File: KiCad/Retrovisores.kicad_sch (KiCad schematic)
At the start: 50 parts, among them J1 Conn_01x02_Pin, J2 Conn_PIC_ICSP_ICD, M1 Motor_DC, M2 Motor_DC, M3 Motor_DC, Q1 AO3400A, Q10 AO3401A, Q11 AO3400A, Q12 AO3401A, Q2 AO3400A, Q3 AO3401A, Q4 AO3401A, Q5 AO3400A, Q6 AO3401A, Q7 AO3400A, Q8 AO3401A, Q9 AO3400A, SW1 SW_SPST, SW10 SW_Push, SW2 SW_SPST, SW3 SW_SPST, SW4 SW_SPST, SW5 SW_SPST, SW6 SW_SPST, SW7 SW_Push, SW8 SW_Push, SW9 SW_Push, U1 PIC32MX250F128D-IPT, U2 SN65HVD232, U3 FT232RL, U4 LT1117-3.3, U5 TSR3-2450N, U6 VL53L1CXV0FY1

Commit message: he ordenat tot
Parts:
- removed C1, C2: C, symbol Device:C
- removed C3: 100 nF, symbol Device:C
- removed D1: LED, symbol Device:LED
- removed J1: Conn_01x02_Pin, symbol Connector:Conn_01x02_Pin
- removed J2: Conn_PIC_ICSP_ICD, symbol Connector:Conn_PIC_ICSP_ICD
- removed M1, M2, M3: Motor_DC, symbol Motor:Motor_DC
- removed Q1, Q11, Q2, Q5, Q7, Q9: AO3400A, Package_TO_SOT_SMD:SOT-23, symbol Transistor_FET:AO3400A
- removed Q10, Q12, Q3, Q4, Q6, Q8: AO3401A, Package_TO_SOT_SMD:SOT-23, symbol Transistor_FET:AO3401A
- removed R1, R10, R11, R12, R2, R3, R4, R5, R6, R7, R8, R9: R, symbol Device:R
- removed R13: 1k, symbol Device:R
- removed SW1, SW2, SW3, SW4, SW5, SW6: SW_SPST, symbol Switch:SW_SPST
- removed SW10, SW7, SW8, SW9: SW_Push, symbol Switch:SW_Push
- removed U1: PIC32MX250F128D-IPT, Package_QFP:TQFP-44_10x10mm_P0.8mm, symbol MCU_Microchip_PIC32:PIC32MX250F128D-IPT
- removed U2: SN65HVD232, Package_SO:SOIC-8_3.9x4.9mm_P1.27mm, symbol Interface_CAN_LIN:SN65HVD232
- removed U3: FT232RL, Package_SO:SSOP-28_5.3x10.2mm_P0.65mm, symbol Interface_USB:FT232RL
- removed U4: LT1117-3.3, symbol Regulator_Linear:LT1117-3.3
- removed U5: TSR3-2450N, Converter_DCDC:Converter_DCDC_TRACO_TSR2-24xxN_TSR2-24xxxN_THT, symbol Converter_DCDC:TSR3-2450N
- removed U6: VL53L1CXV0FY1, Sensor_Distance:ST_VL53L1x, symbol Sensor_Distance:VL53L1CXV0FY1
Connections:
- no-connect marks 2 -> 0
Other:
- added sheet Alimentacion (alimentacion.kicad_sch)
- added sheet BOTONERA (BOTONERA.kicad_sch)
- added sheet CAN (BUS CAN.kicad_sch)
- added sheet FINALCARRERA (FC.kicad_sch)
- added sheet MICRO (MICRO.kicad_sch)
- added sheet PROGRAMADOR (PROGRAMADOR.kicad_sch)
- added sheet SENSOR (SENSOR_PROX_sch.kicad_sch)
- added sheet USART (USART.kicad_sch)
- added sheet drivers motor (driver_sch.kicad_sch)

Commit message: calefactor
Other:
- added sheet Calefactor (Calefactor_sch.kicad_sch)
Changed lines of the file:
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@@
 	(paper "A4")
+	(sheet
+		(at 153.67 58.42)
+		(size 35.56 20.32)
+		(exclude_from_sim no)
+		(in_bom yes)
+		(on_board yes)
+		(dnp no)
+		(fields_autoplaced yes)
+		(stroke
+			(width 0.1524)
+			(type solid)
+		)
+		(fill
+			(color 0 0 0 0.0000)
+		)
+		(property "Sheetname" "Calefactor"
+			(at 153.67 57.7084 0)
+			(effects
+				(font
+					(size 1.27 1.27)
+				)
+				(justify left bottom)
+			)
+		)
+		(property "Sheetfile" "Calefactor_sch.kicad_sch"
+			(at 153.67 79.3246 0)
+			(effects
+				(font
+					(size 1.27 1.27)
+				)
+				(justify left top)
+			)
+		)
+		(instances
+			(project "Retrovisores"
+				(path "/9b9f005f-0621-4675-bd4e-683e7082b120"
+					(page "11")
+				)
+			)
+		)
+	)
 	(sheet
 		(at 67.31 24.13)

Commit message: calefactor-Usart
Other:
- removed sheet USART
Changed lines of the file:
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@@
-		)
-	)
-	(sheet
-		(at 237.49 24.13)
-		(size 34.29 22.86)
-		(exclude_from_sim no)
-		(in_bom yes)
-		(on_board yes)
-		(dnp no)
-		(fields_autoplaced yes)
-		(stroke
-			(width 0.1524)
-			(type solid)
-		)
-		(fill
-			(color 0 0 0 0.0000)
-		)
-		(property "Sheetname" "USART"
-			(at 237.49 23.4184 0)
-			(effects
-				(font
-					(size 1.27 1.27)
-				)
-				(justify left bottom)
-			)
-		)
-		(property "Sheetfile" "USART.kicad_sch"
-			(at 237.49 47.5746 0)
-			(effects
-				(font
-					(size 1.27 1.27)
-				)
-				(justify left top)
-			)
-		)
-		(instances
-			(project "Retrovisores"
-				(path "/9b9f005f-0621-4675-bd4e-683e7082b120"
-					(page "7")
-				)
-			)
 		)
 	)

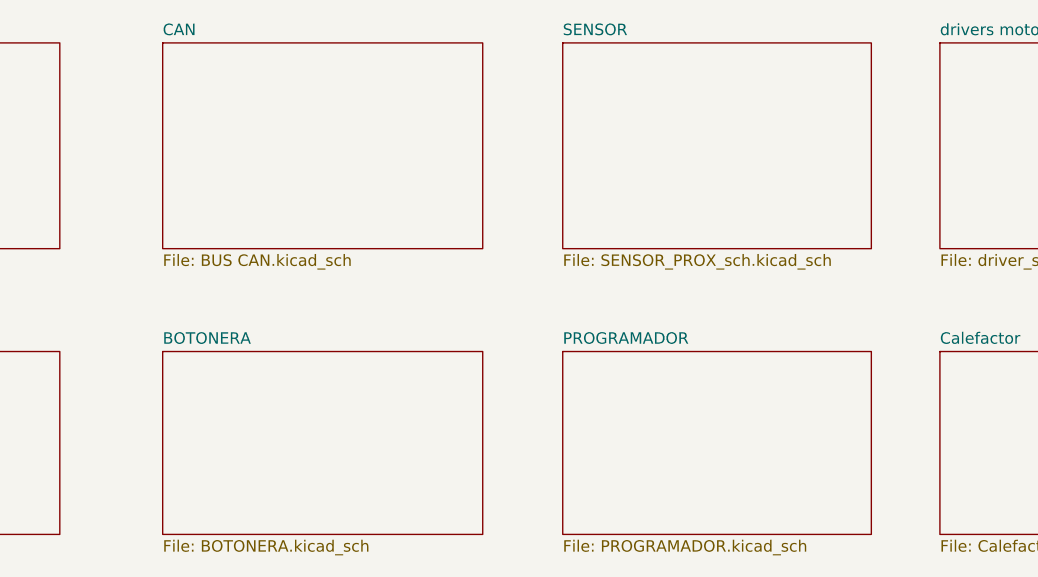
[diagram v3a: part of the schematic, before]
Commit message: canvis organització y reles calefactor
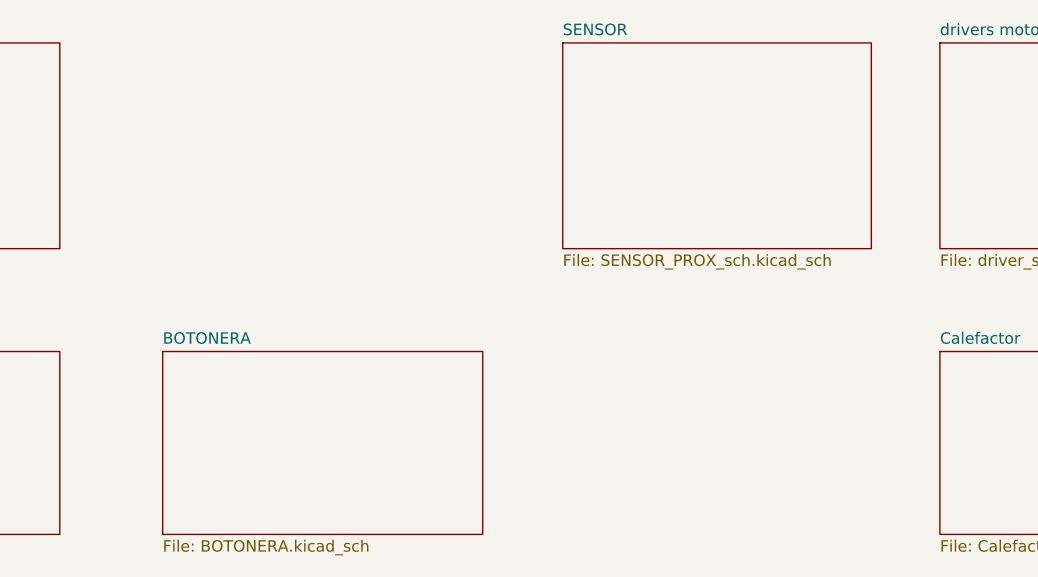
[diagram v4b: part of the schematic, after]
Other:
- removed sheet CAN
- removed sheet PROGRAMADOR
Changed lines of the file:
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@@
-	)
-	(sheet
-		(at 67.31 24.13)
-		(size 35.56 22.86)
-		(exclude_from_sim no)
-		(in_bom yes)
-		(on_board yes)
-		(dnp no)
-		(fields_autoplaced yes)
-		(stroke
-			(width 0.1524)
-			(type solid)
-		)
-		(fill
-			(color 0 0 0 0.0000)
-		)
-		(property "Sheetname" "CAN"
-			(at 67.31 23.4184 0)
-			(effects
-				(font
-					(size 1.27 1.27)
-				)
-				(justify left bottom)
-			)
-		)
-		(property "Sheetfile" "BUS CAN.kicad_sch"
-			(at 67.31 47.5746 0)
-			(effects
-				(font
-					(size 1.27 1.27)
-				)
-				(justify left top)
-			)
-		)
-		(instances
-			(project "Retrovisores"
-				(path "/9b9f005f-0621-4675-bd4e-683e7082b120"
-					(page "3")
-				)
-			)
-		)
 	)
 	(sheet
@@
 				)
 			)
-		)
-	)
-	(sheet
-		(at 111.76 58.42)
-		(size 34.29 20.32)
-		(exclude_from_sim no)
-		(in_bom yes)
-		(on_board yes)
-		(dnp no)
-		(fields_autoplaced yes)
-		(stroke
-			(width 0.1524)
-			(type solid)
-		)
-		(fill
-			(color 0 0 0 0.0000)
-		)
-		(property "Sheetname" "PROGRAMADOR"
-			(at 111.76 57.7084 0)
-			(effects
-				(font
-					(size 1.27 1.27)
-				)
-				(justify left bottom)
-			)
-		)
-		(property "Sheetfile" "PROGRAMADOR.kicad_sch"
-			(at 111.76 79.3246 0)
-			(effects
-				(font
-					(size 1.27 1.27)
-				)
-				(justify left top)
-			)
-		)
-		(instances
-			(project "Retrovisores"
-				(path "/9b9f005f-0621-4675-bd4e-683e7082b120"
-					(page "10")
-				)
-			)

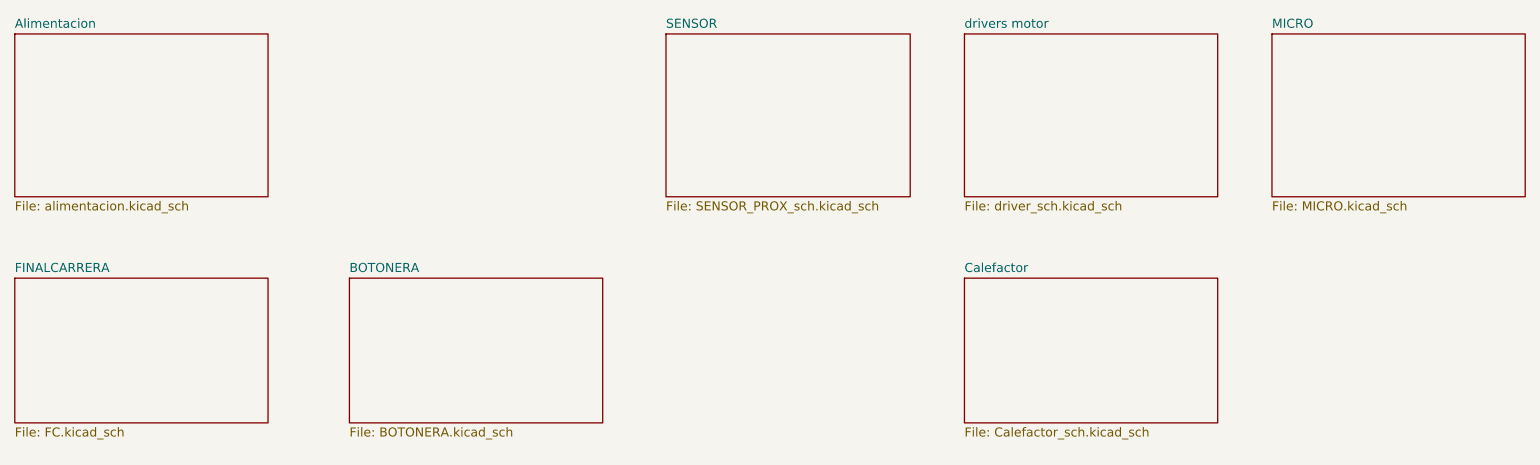
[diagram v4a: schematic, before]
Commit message: reorganizado el esquematico
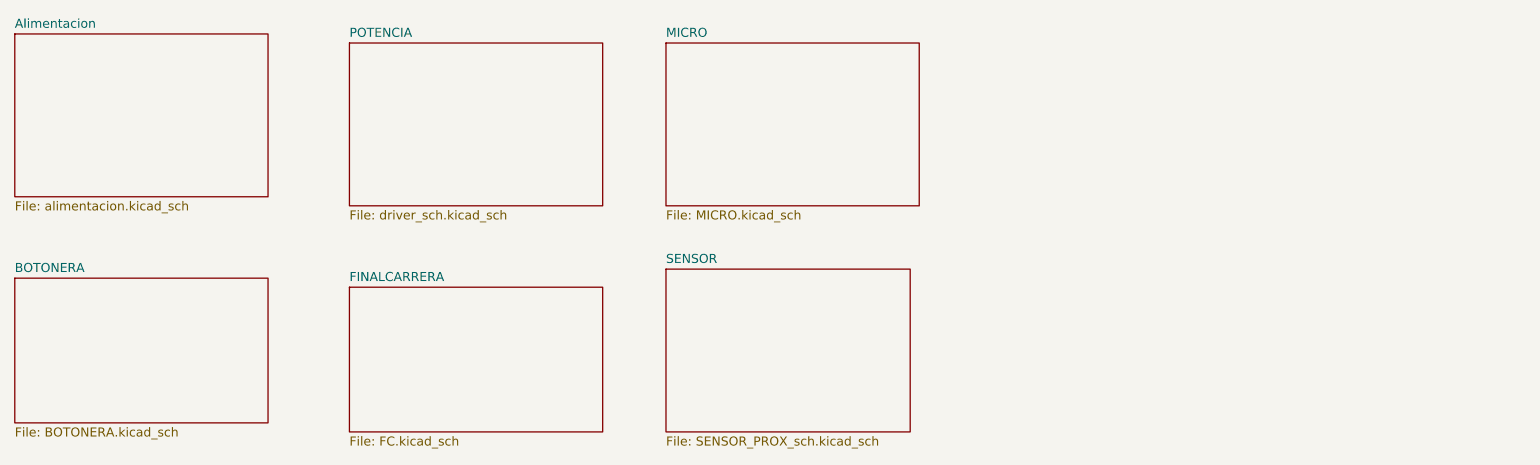
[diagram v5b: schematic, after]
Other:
- sheet drivers motor renamed POTENCIA
- removed sheet Calefactor
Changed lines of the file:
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@@
 	(paper "A4")
 	(sheet
-		(at 153.67 58.42)
+		(at 111.76 25.4)
+		(size 35.56 22.86)
+		(exclude_from_sim no)
+		(in_bom yes)
+		(on_board yes)
+		(dnp no)
+		(fields_autoplaced yes)
+		(stroke
+			(width 0.1524)
+			(type solid)
+		)
+		(fill
+			(color 0 0 0 0.0000)
+		)
+		(property "Sheetname" "MICRO"
+			(at 111.76 24.6884 0)
+			(effects
+				(font
+					(size 1.27 1.27)
+				)
+				(justify left bottom)
+			)
+		)
+		(property "Sheetfile" "MICRO.kicad_sch"
+			(at 111.76 48.8446 0)
+			(effects
+				(font
+					(size 1.27 1.27)
+				)
+				(justify left top)
+			)
+		)
+		(instances
+			(project "Retrovisores"
+				(path "/9b9f005f-0621-4675-bd4e-683e7082b120"
+					(page "6")
+				)
+			)
+		)
+	)
+	(sheet
+		(at 67.31 59.69)
 		(size 35.56 20.32)
 		(exclude_from_sim no)
@@
 			(color 0 0 0 0.0000)
 		)
-		(property "Sheetname" "Calefactor"
-			(at 153.67 57.7084 0)
-			(effects
-				(font
-					(size 1.27 1.27)
-				)
-				(justify left bottom)
-			)
-		)
-		(property "Sheetfile" "Calefactor_sch.kicad_sch"
-			(at 153.67 79.3246 0)
-			(effects
-				(font
-					(size 1.27 1.27)
-				)
-				(justify left top)
-			)
-		)
-		(instances
-			(project "Retrovisores"
-				(path "/9b9f005f-0621-4675-bd4e-683e7082b120"
-					(page "11")
-				)
-			)
-		)
-	)
-	(sheet
-		(at 196.85 24.13)
+		(property "Sheetname" "FINALCARRERA"
+			(at 67.31 58.9784 0)
+			(effects
+				(font
+					(size 1.27 1.27)
+				)
+				(justify left bottom)
+			)
+		)
+		(property "Sheetfile" "FC.kicad_sch"
+			(at 67.31 80.5946 0)
+			(effects
+				(font
+					(size 1.27 1.27)
+				)
+				(justify left top)
+			)
+		)
+		(instances
+			(project "Retrovisores"
+				(path "/9b9f005f-0621-4675-bd4e-683e7082b120"
+					(page "8")
+				)
+			)
+		)
+	)
+	(sheet
+		(at 111.76 57.15)
+		(size 34.29 22.86)
+		(exclude_from_sim no)
+		(in_bom yes)
+		(on_board yes)
+		(dnp no)
+		(fields_autoplaced yes)
+		(stroke
+			(width 0.1524)
+			(type solid)
+		)
+		(fill
+			(color 0 0 0 0.0000)
+		)
+		(property "Sheetname" "SENSOR"
+			(at 111.76 56.4384 0)
+			(effects
+				(font
+					(size 1.27 1.27)
+				)
+				(justify left bottom)
+			)
+		)
+		(property "Sheetfile" "SENSOR_PROX_sch.kicad_sch"
+			(at 111.76 80.5946 0)
+			(effects
+				(font
+					(size 1.27 1.27)
+				)
+				(justify left top)
+			)
+		)
+		(instances
+			(project "Retrovisores"
+				(path "/9b9f005f-0621-4675-bd4e-683e7082b120"
+					(page "4")
+				)
+			)
+		)
+	)
+	(sheet
+		(at 20.32 24.13)
 		(size 35.56 22.86)
 		(exclude_from_sim no)
@@
 			(color 0 0 0 0.0000)
 		)
-		(property "Sheetname" "MICRO"
-			(at 196.85 23.4184 0)
-			(effects
-				(font
-					(size 1.27 1.27)
-				)
-				(justify left bottom)
-			)
-		)
-		(property "Sheetfile" "MICRO.kicad_sch"
-			(at 196.85 47.5746 0)
-			(effects
-				(font
-					(size 1.27 1.27)
-				)
-				(justify left top)
-			)
-		)
-		(instances
-			(project "Retrovisores"
-				(path "/9b9f005f-0621-4675-bd4e-683e7082b120"
-					(page "6")
+		(property "Sheetname" "Alimentacion"
+			(at 20.32 23.4184 0)
+			(effects
+				(font
+					(size 1.27 1.27)
+				)
+				(justify left bottom)
+			)
+		)
+		(property "Sheetfile" "alimentacion.kicad_sch"
+			(at 20.32 47.5746 0)
+			(effects
+				(font
+					(size 1.27 1.27)
+				)
+				(justify left top)
+			)
+		)
+		(instances
+			(project "Retrovisores"
+				(path "/9b9f005f-0621-4675-bd4e-683e7082b120"
+					(page "2")
+				)
+			)
+		)
+	)
+	(sheet
+		(at 67.31 25.4)
+		(size 35.56 22.86)
+		(exclude_from_sim no)
+		(in_bom yes)
+		(on_board yes)
+		(dnp no)
+		(fields_autoplaced yes)
+		(stroke
+			(width 0.1524)
+			(type solid)
+		)
+		(fill
+			(color 0 0 0 0.0000)
+		)
+		(property "Sheetname" "POTENCIA"
+			(at 67.31 24.6884 0)
+			(effects
+				(font
+					(size 1.27 1.27)
+				)
+				(justify left bottom)
+			)
+		)
+		(property "Sheetfile" "driver_sch.kicad_sch"
+			(at 67.31 48.8446 0)
+			(effects
+				(font
+					(size 1.27 1.27)
+				)
+				(justify left top)
+			)
+		)
+		(instances
+			(project "Retrovisores"
+				(path "/9b9f005f-0621-4675-bd4e-683e7082b120"
+					(page "5")
 				)
 			)
@@
 			(color 0 0 0 0.0000)
 		)
-		(property "Sheetname" "FINALCARRERA"
+		(property "Sheetname" "BOTONERA"
 			(at 20.32 57.7084 0)
 			(effects
@@
 			)
 		)
-		(property "Sheetfile" "FC.kicad_sch"
+		(property "Sheetfile" "BOTONERA.kicad_sch"
 			(at 20.32 79.3246 0)
 			(effects
 				(font
-					(size 1.27 1.27)
-				)
-				(justify left top)
-			)
-		)
-		(instances
-			(project "Retrovisores"
-				(path "/9b9f005f-0621-4675-bd4e-683e7082b120"
-					(page "8")
-				)
-			)
-		)
-	)
-	(sheet
-		(at 111.76 24.13)
-		(size 34.29 22.86)
-		(exclude_from_sim no)
-		(in_bom yes)
-		(on_board yes)
-		(dnp no)
-		(fields_autoplaced yes)
-		(stroke
-			(width 0.1524)
-			(type solid)
-		)
-		(fill
-			(color 0 0 0 0.0000)
-		)
-		(property "Sheetname" "SENSOR"
-			(at 111.76 23.4184 0)
-			(effects
-				(font
-					(size 1.27 1.27)
-				)
-				(justify left bottom)
-			)
-		)
-		(property "Sheetfile" "SENSOR_PROX_sch.kicad_sch"
-			(at 111.76 47.5746 0)
-			(effects
-				(font
-					(size 1.27 1.27)
-				)
-				(justify left top)
-			)
-		)
-		(instances
-			(project "Retrovisores"
-				(path "/9b9f005f-0621-4675-bd4e-683e7082b120"
-					(page "4")
-				)
-			)
-		)
-	)
-	(sheet
-		(at 20.32 24.13)
-		(size 35.56 22.86)
-		(exclude_from_sim no)
-		(in_bom yes)
-		(on_board yes)
-		(dnp no)
-		(fields_autoplaced yes)
-		(stroke
-			(width 0.1524)
-			(type solid)
-		)
-		(fill
-			(color 0 0 0 0.0000)
-		)
-		(property "Sheetname" "Alimentacion"
-			(at 20.32 23.4184 0)
-			(effects
-				(font
-					(size 1.27 1.27)
-				)
-				(justify left bottom)
-			)
-		)
-		(property "Sheetfile" "alimentacion.kicad_sch"
-			(at 20.32 47.5746 0)
-			(effects
-				(font
-					(size 1.27 1.27)
-				)
-				(justify left top)
-			)
-		)
-		(instances
-			(project "Retrovisores"
-				(path "/9b9f005f-0621-4675-bd4e-683e7082b120"
-					(page "2")
-				)
-			)
-		)
-	)
-	(sheet
-		(at 153.67 24.13)
-		(size 35.56 22.86)
-		(exclude_from_sim no)
-		(in_bom yes)
-		(on_board yes)
-		(dnp no)
-		(fields_autoplaced yes)
-		(stroke
-			(width 0.1524)
-			(type solid)
-		)
-		(fill
-			(color 0 0 0 0.0000)
-		)
-		(property "Sheetname" "drivers motor"
-			(at 153.67 23.4184 0)
-			(effects
-				(font
-					(size 1.27 1.27)
-				)
-				(justify left bottom)
-			)
-		)
-		(property "Sheetfile" "driver_sch.kicad_sch"
-			(at 153.67 47.5746 0)
-			(effects
-				(font
-					(size 1.27 1.27)
-				)
-				(justify left top)
-			)
-		)
-		(instances
-			(project "Retrovisores"
-				(path "/9b9f005f-0621-4675-bd4e-683e7082b120"
-					(page "5")
-				)
-			)
-		)
-	)
-	(sheet
-		(at 67.31 58.42)
-		(size 35.56 20.32)
-		(exclude_from_sim no)
-		(in_bom yes)
-		(on_board yes)
-		(dnp no)
-		(fields_autoplaced yes)
-		(stroke
-			(width 0.1524)
-			(type solid)
-		)
-		(fill
-			(color 0 0 0 0.0000)
-		)
-		(property "Sheetname" "BOTONERA"
-			(at 67.31 57.7084 0)
-			(effects
-				(font
-					(size 1.27 1.27)
-				)
-				(justify left bottom)
-			)
-		)
-		(property "Sheetfile" "BOTONERA.kicad_sch"
-			(at 67.31 79.3246 0)
-			(effects
-				(font
